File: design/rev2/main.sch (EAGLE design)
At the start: 44 parts, among them J1 ICSP-HEADER1X6-0.1-ICSP-PADS, J2 HEADER-141X14-0.05-PADS, SW1 B3U-3000P, U1 PIC18F2XK20, U2 LIS3DSH, U3 APDS-9008, U4 APDS-9008

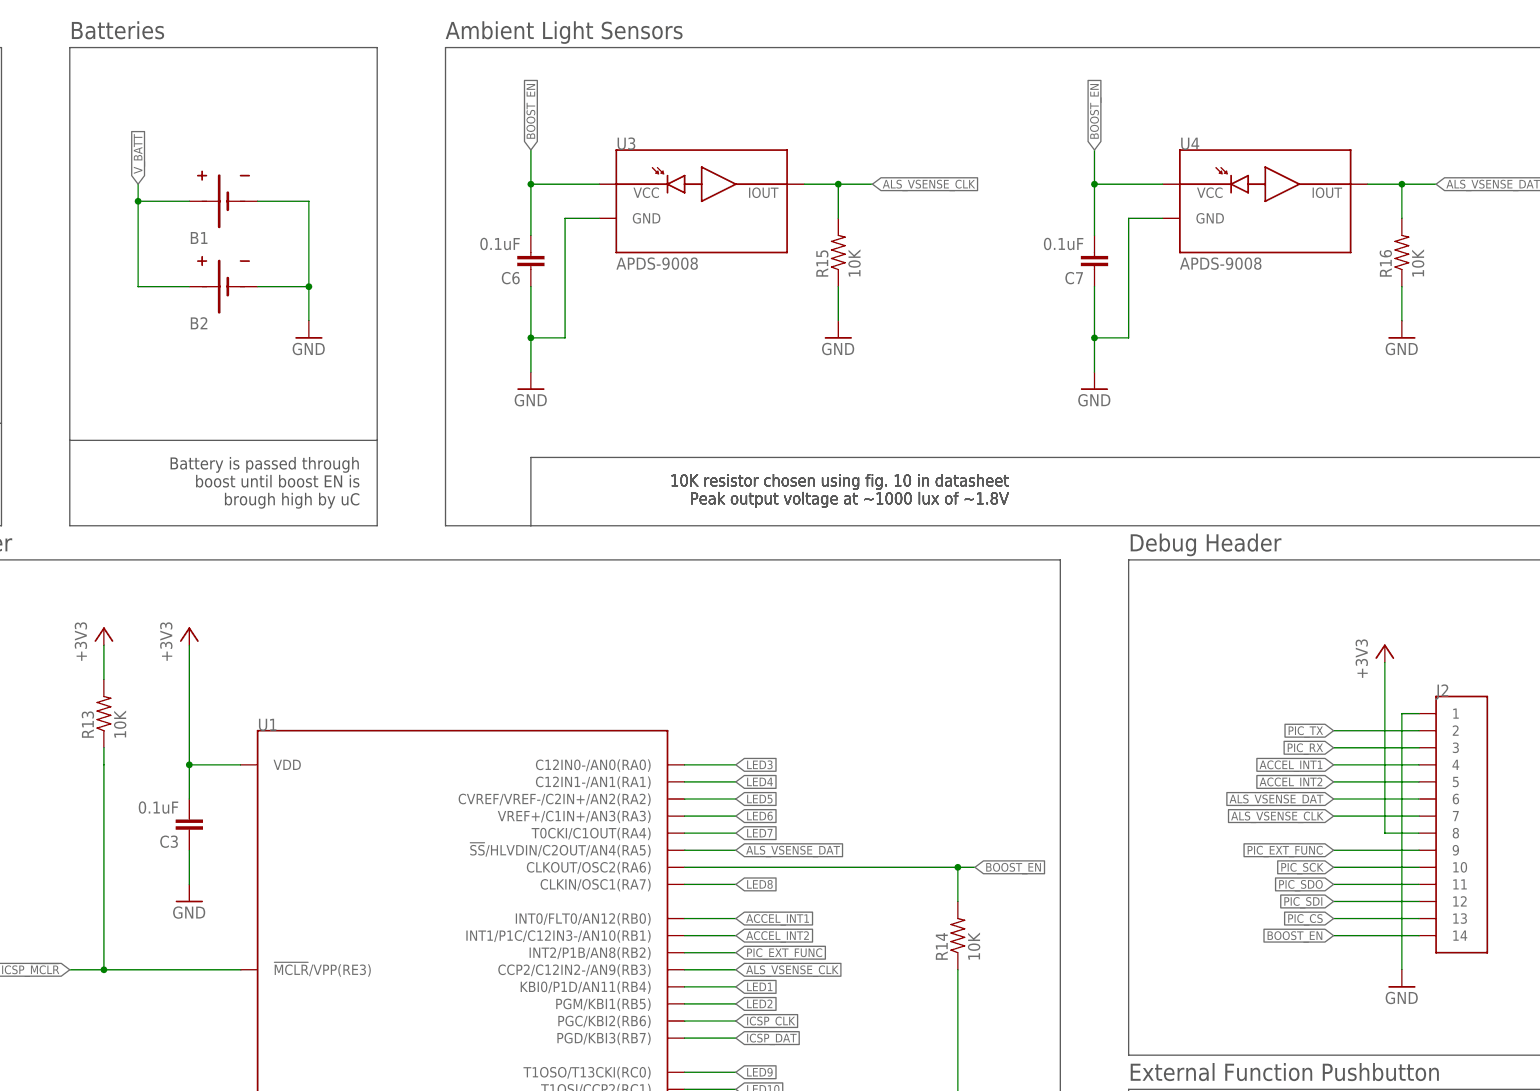
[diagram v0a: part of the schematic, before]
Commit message: [CNG] - finished most routing on rev2, added new mechanical drawings (not up to date with POR)
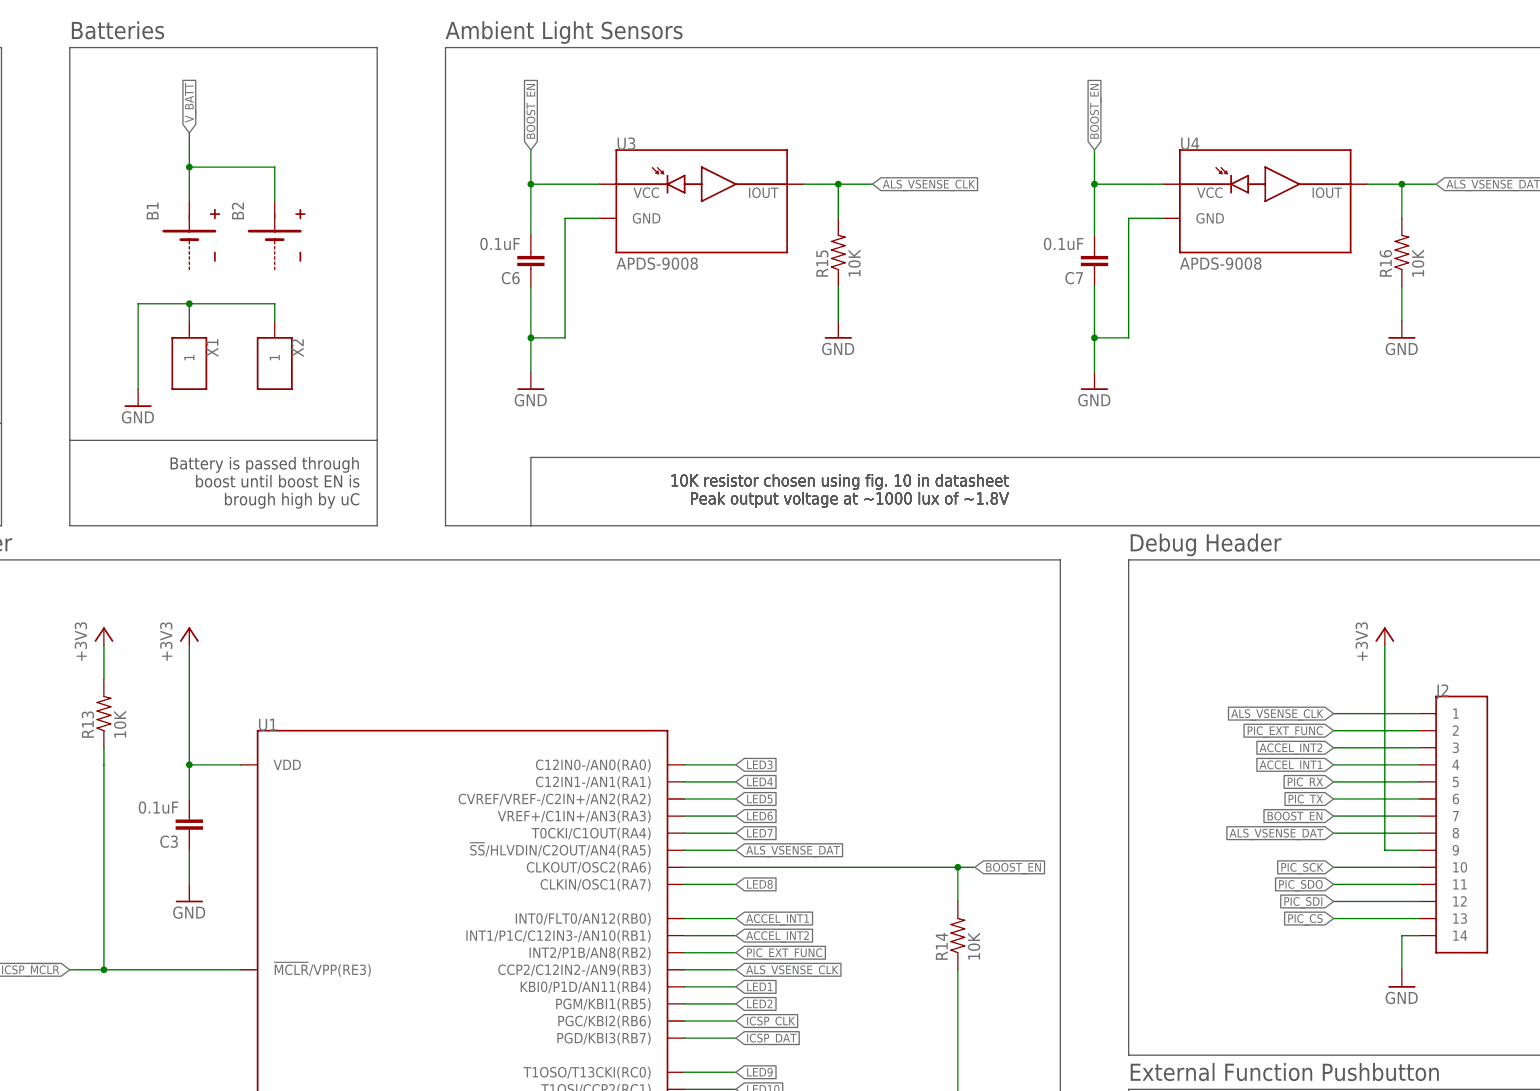
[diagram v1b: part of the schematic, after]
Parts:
- added X1, X2: TE-2199248-X, matt:TE-2199248-X
- B1, B2: value BATTERYCR-2016/F2N -> BATTERY-POS-HALF; device matt:BATTERYCR-2016/F2N -> matt:BATTERY-POS-HALF
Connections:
- net +3V3: now also J2.9; no longer J2.8
- net ACCEL_INT2: now also J2.3; no longer J2.5
- net ALS_VSENSE_CLK: now also J2.1; no longer J2.7
- net ALS_VSENSE_DAT: now also J2.8; no longer J2.6
- net BOOST_EN: now also J2.7; no longer J2.14
- net GND: now also J2.14, X1.1, X2.1; no longer B1.P$-, B2.P$-, J2.1
- net PIC_EXT_FUNC: now also J2.2; no longer J2.9
- net PIC_RX: now also J2.5; no longer J2.3
- net PIC_TX: now also J2.6; no longer J2.2
